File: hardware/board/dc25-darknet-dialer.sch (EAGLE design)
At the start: 80 parts, among them SW1 RESET, X1 USB-MICROB

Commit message: Connected LEDs
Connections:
- net N$57 renamed IR_RCV
- removed net N$46 (its old number): U$2.PC11
- removed net N$47: U$2.PC10
- removed net N$48 (its old number): U$2.PA15
- removed net N$50: U$2.PC9
- removed net N$51: U$2.PC8
- removed net N$52: U$2.PC7
- removed net N$53: U$2.PC6
- removed net N$54: U$2.PC14
- removed net N$58: U$2.PC1
- removed net N$59: U$2.PC2
- removed net N$60: U$2.PC3
- removed net N$61 (its old number): U$2.PB10
- removed net N$62: U$12.LED
- new net OLED_CS: U$12.CS, U$2.PC6
- new net OLED_LED: U$12.LED, U$2.PC7
- net LED1: now also U$2.PC9
- net LED10: now also U$2.PA15
- net LED2: now also U$2.PC8
- net LED3: now also U$2.PB10
- net LED4: now also U$2.PC3
- net LED5: now also U$2.PC2
- net LED6: now also U$2.PC1
- net LED7: now also U$2.PC14
- net LED8: now also U$2.PC11
- net LED9: now also U$2.PC10
- net VCC: no longer U$12.CS

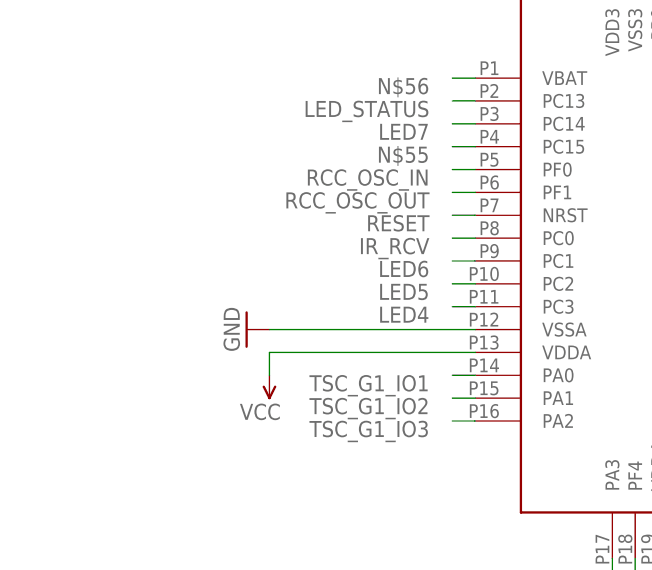
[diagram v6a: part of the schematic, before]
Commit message: Added resonator
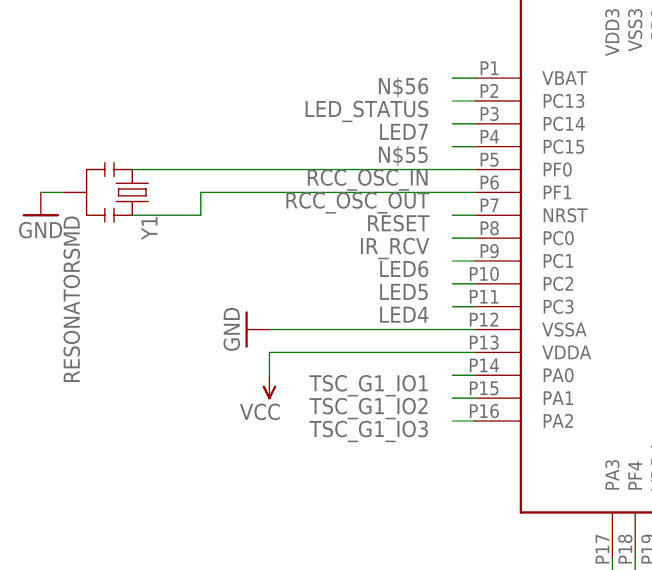
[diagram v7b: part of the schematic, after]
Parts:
- added Y1: RESONATORSMD, SparkFun:RESONATORSMD
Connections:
- net GND: now also Y1.2
- net RCC_OSC_IN: now also Y1.1
- net RCC_OSC_OUT: now also Y1.3
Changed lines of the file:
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@@
 <part name="L1" library="dp_devices" deviceset="FERRITE" device="-0603"/>
 <part name="GND26" library="SYNShop" deviceset="GND" device=""/>
+<part name="Y1" library="SparkFun" deviceset="RESONATOR" device="SMD"/>
+<part name="GND29" library="SYNShop" deviceset="GND" device=""/>
 </parts>
 <sheets>
@@
 <instance part="L1" gate="L" x="15.24" y="363.22" rot="R90"/>
 <instance part="GND26" gate="1" x="33.02" y="355.6"/>
+<instance part="Y1" gate="G$1" x="-43.18" y="104.14" rot="R270"/>
+<instance part="GND29" gate="1" x="-53.34" y="101.6"/>
 </instances>
 <busses>
@@
 <pinref part="SW1" gate="G$1" pin="C"/>
 </segment>
+<segment>
+<pinref part="Y1" gate="G$1" pin="2"/>
+<wire x1="-50.8" y1="104.14" x2="-53.34" y2="104.14" width="0.1524" layer="91"/>
+<pinref part="GND29" gate="1" pin="GND"/>
+</segment>
 </net>
 <net name="N$12" class="0">
@@
 <segment>
 <pinref part="U$2" gate="G$1" pin="PF0"/>
-<wire x1="-5.08" y1="106.68" x2="-7.62" y2="106.68" width="0.1524" layer="91"/>
 <label x="-10.16" y="106.68" size="1.778" layer="95" rot="R180"/>
+<pinref part="Y1" gate="G$1" pin="1"/>
+<wire x1="-5.08" y1="106.68" x2="-43.18" y2="106.68" width="0.1524" layer="91"/>
 </segment>
 </net>
@@
 <segment>
 <pinref part="U$2" gate="G$1" pin="PF1"/>
-<wire x1="-5.08" y1="104.14" x2="-7.62" y2="104.14" width="0.1524" layer="91"/>
 <label x="-10.16" y="104.14" size="1.778" layer="95" rot="R180"/>
-</segment>
-</net>
+<wire x1="-5.08" y1="104.14" x2="-35.56" y2="104.14" width="0.1524" layer="91"/>
+<wire x1="-35.56" y1="104.14" x2="-35.56" y2="101.6" width="0.1524" layer="91"/>
+<pinref part="Y1" gate="G$1" pin="3"/>
+<wire x1="-35.56" y1="101.6" x2="-43.18" y2="101.6" width="0.1524" layer="91"/>
+</segment>
+</net>

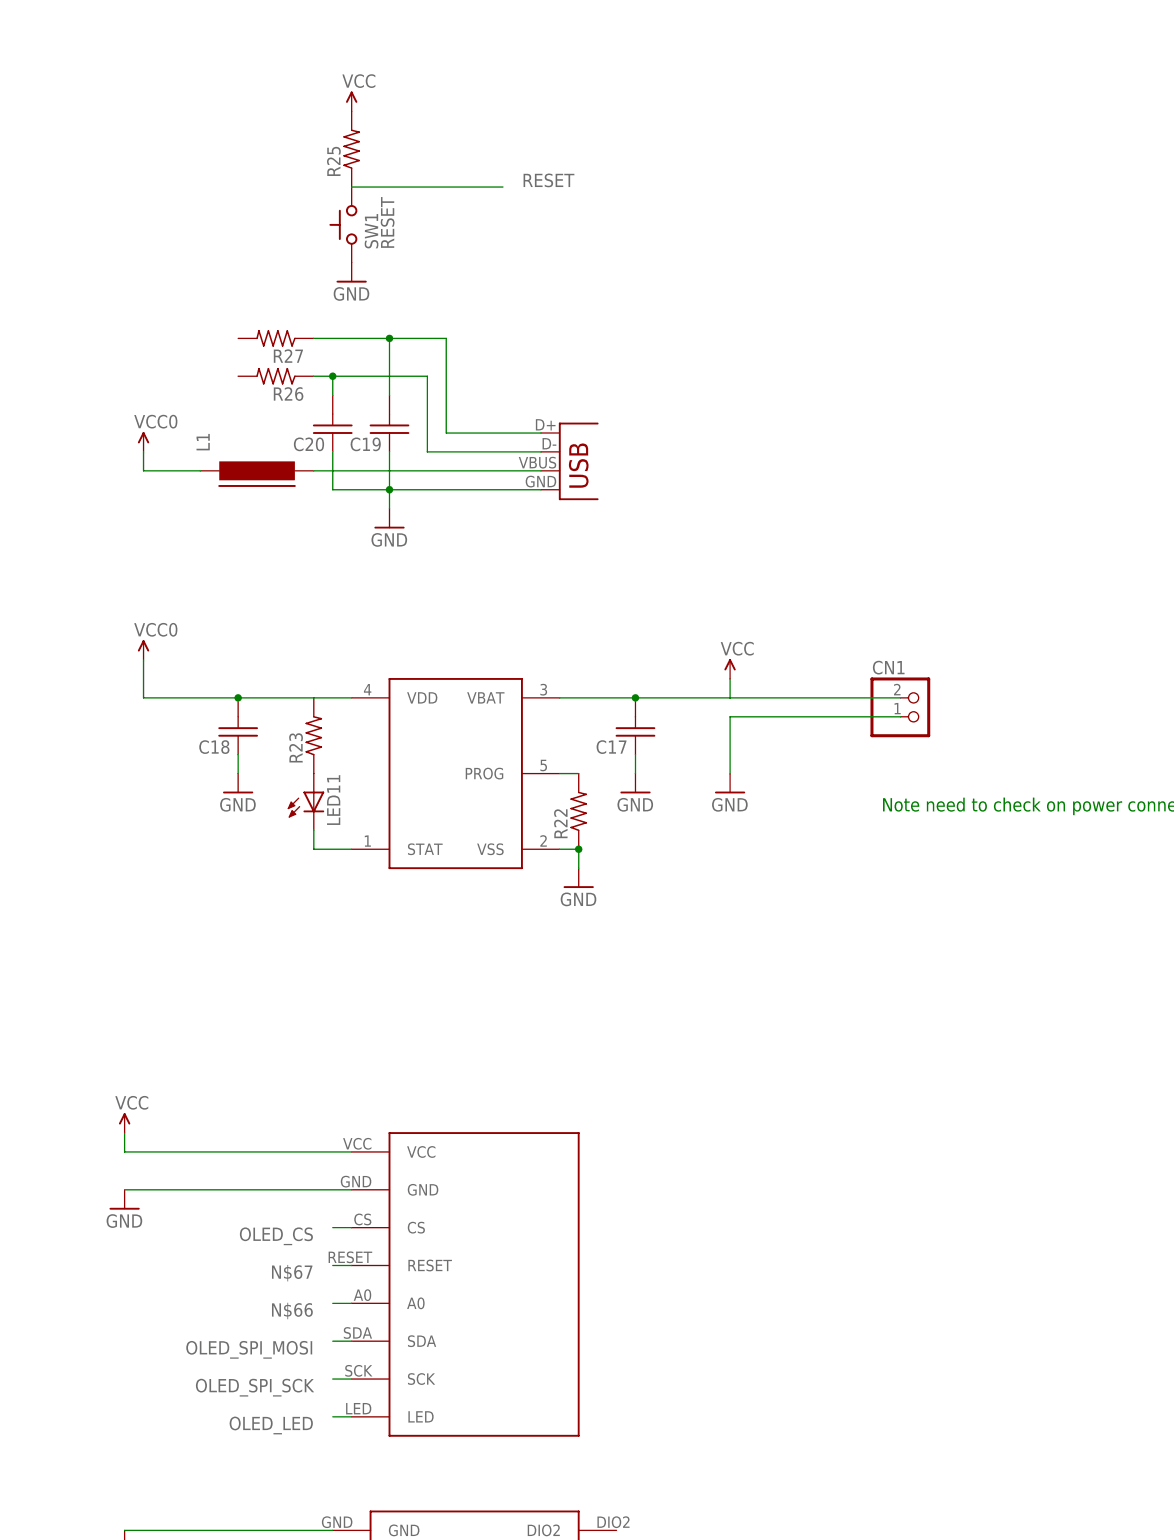
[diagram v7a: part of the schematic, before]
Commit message: Additional details on power, added fuse and prep for 3.3v LDO
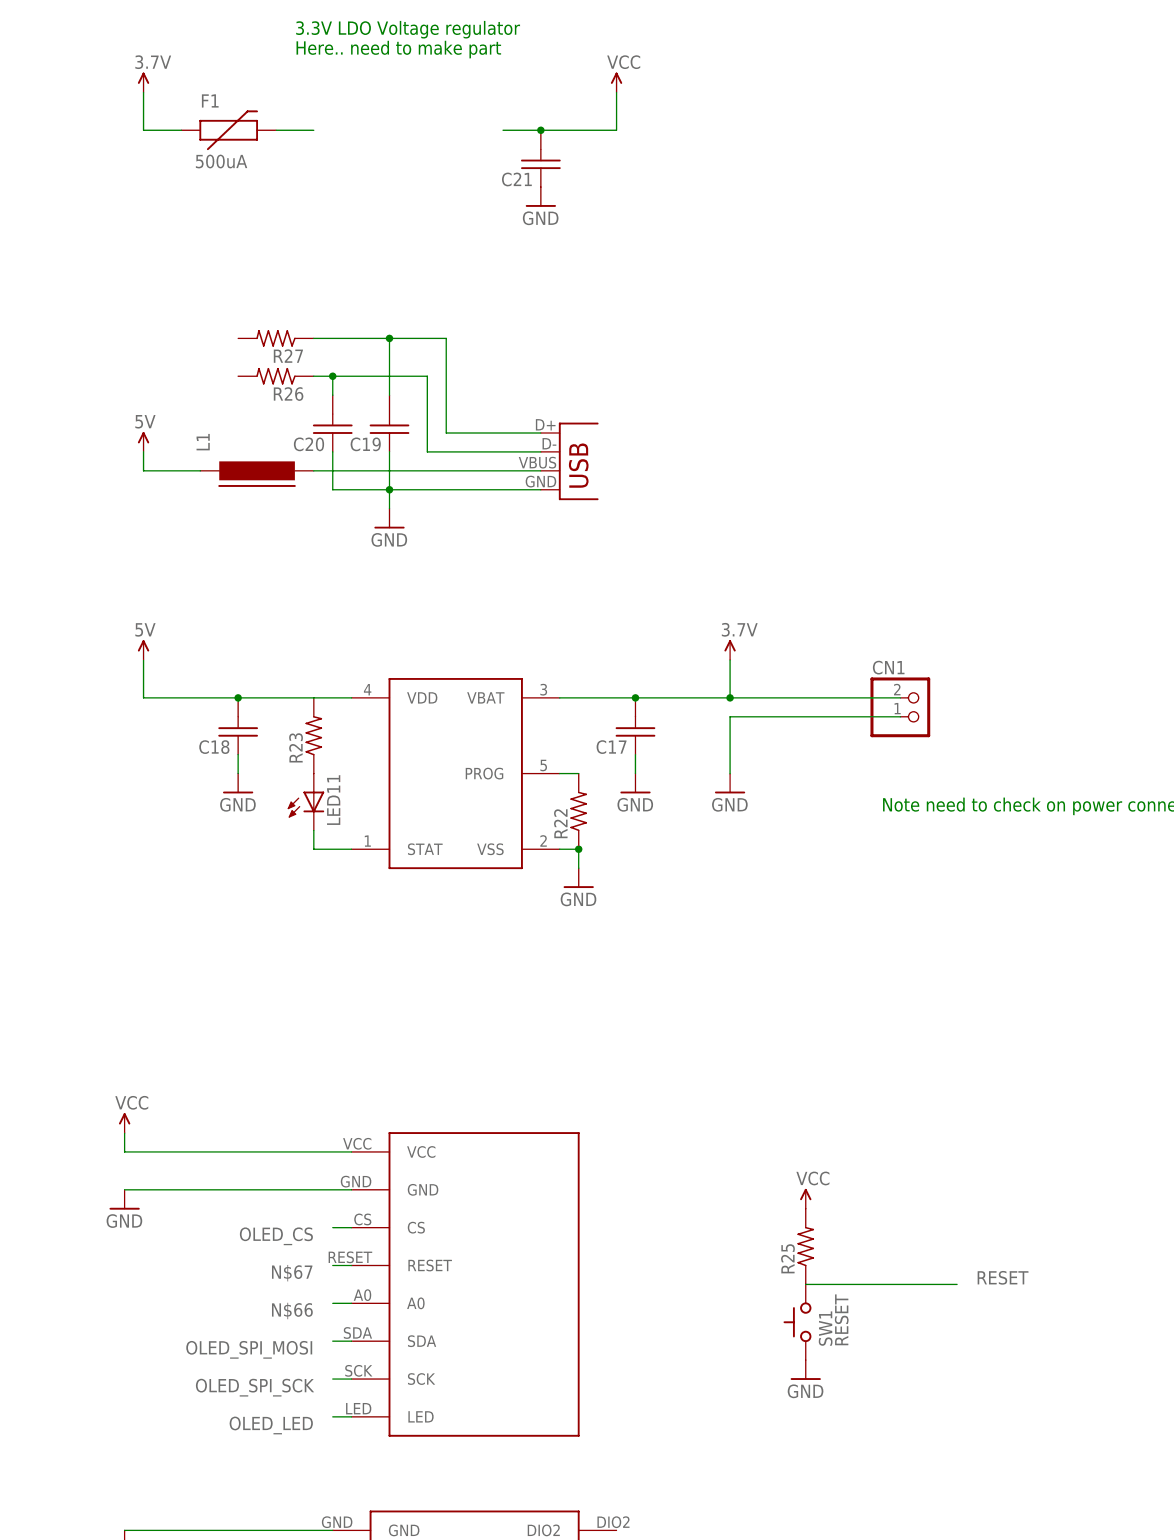
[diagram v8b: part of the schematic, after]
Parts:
- added C21: (no value), SYNShop:C-USC0603
- added F1: 500uA, SparkFun:PTCSMD
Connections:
- new net N$31: F1.2
- new net VCC1: C17.2, CN1.1, F1.1, U$11.VBAT
- net GND: now also C21.1
- net VCC: now also C21.2; no longer C17.2, CN1.1, U$11.VBAT
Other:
- note added: "3.3V LDO Voltage regulator Here.. need to make part"
- moved on the sheet: R25, SW1
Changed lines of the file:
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@@
 <part name="C17" library="SYNShop" deviceset="C-US" device="C0603"/>
 <part name="GND24" library="SYNShop" deviceset="GND" device=""/>
-<part name="U$13" library="SYNShop" deviceset="VCC" device=""/>
-<part name="U$14" library="SYNShop" deviceset="VCC0" device=""/>
+<part name="5V" library="SYNShop" deviceset="VCC0" device="" value="5V"/>
 <part name="C18" library="SYNShop" deviceset="C-US" device="C0603"/>
 <part name="GND25" library="SYNShop" deviceset="GND" device=""/>
 <part name="X1" library="SYNShop" deviceset="USB" device="-MICROB"/>
-<part name="U$16" library="SYNShop" deviceset="VCC0" device=""/>
+<part name="U$16" library="SYNShop" deviceset="VCC0" device="" value="5V"/>
 <part name="U$17" library="SYNShop" deviceset="SOP22" device=""/>
 <part name="LED12" library="SYNShop" deviceset="LED" device="5MM"/>
@@
 <part name="Y1" library="SparkFun" deviceset="RESONATOR" device="SMD"/>
 <part name="GND29" library="SYNShop" deviceset="GND" device=""/>
+<part name="3.7V" library="SYNShop" deviceset="VCC1" device="" value="3.7V"/>
+<part name="F1" library="SparkFun" deviceset="PTC" device="SMD" value="500uA"/>
+<part name="3.7V1" library="SYNShop" deviceset="VCC1" device="" value="3.7V"/>
+<part name="C21" library="SYNShop" deviceset="C-US" device="C0603"/>
+<part name="GND30" library="SYNShop" deviceset="GND" device=""/>
+<part name="U$13" library="SYNShop" deviceset="VCC" device=""/>
 </parts>
 <sheets>
@@
 <plain>
 <text x="99.06" y="317.5" size="1.778" layer="91">Note need to check on power connection / battery</text>
+<text x="20.32" y="419.1" size="1.778" layer="91">3.3V LDO Voltage regulator
+Here.. need to make part</text>
 </plain>
 <instances>
@@
 <instance part="C17" gate="G$1" x="66.04" y="327.66" rot="R180"/>
 <instance part="GND24" gate="1" x="78.74" y="320.04"/>
-<instance part="U$13" gate="G$1" x="78.74" y="335.28"/>
-<instance part="U$14" gate="VCC0" x="0" y="337.82"/>
+<instance part="5V" gate="VCC0" x="0" y="337.82"/>
 <instance part="C18" gate="G$1" x="12.7" y="327.66" rot="R180"/>
 <instance part="GND25" gate="1" x="12.7" y="320.04"/>
@@
 <instance part="U$18" gate="G$1" x="200.66" y="254"/>
 <instance part="CN1" gate="G$1" x="104.14" y="330.2"/>
-<instance part="SW1" gate="G$1" x="27.94" y="396.24"/>
-<instance part="R25" gate="G$1" x="27.94" y="406.4" rot="R90"/>
-<instance part="GND28" gate="1" x="27.94" y="388.62"/>
-<instance part="U$20" gate="G$1" x="27.94" y="411.48"/>
+<instance part="SW1" gate="G$1" x="88.9" y="248.92"/>
+<instance part="R25" gate="G$1" x="88.9" y="259.08" rot="R90"/>
+<instance part="GND28" gate="1" x="88.9" y="241.3"/>
+<instance part="U$20" gate="G$1" x="88.9" y="264.16"/>
 <instance part="R26" gate="G$1" x="17.78" y="375.92" rot="R180"/>
 <instance part="R27" gate="G$1" x="17.78" y="381" rot="R180"/>
@@
 <instance part="Y1" gate="G$1" x="-43.18" y="104.14" rot="R270"/>
 <instance part="GND29" gate="1" x="-53.34" y="101.6"/>
+<instance part="3.7V" gate="G$1" x="78.74" y="337.82"/>
+<instance part="F1" gate="G$1" x="10.16" y="408.94"/>
+<instance part="3.7V1" gate="G$1" x="0" y="414.02"/>
+<instance part="C21" gate="G$1" x="53.34" y="403.86" rot="R180"/>
+<instance part="GND30" gate="1" x="53.34" y="398.78"/>
+<instance part="U$13" gate="G$1" x="63.5" y="414.02"/>
 </instances>
 <busses>
@@
 <pinref part="GND29" gate="1" pin="GND"/>
 </segment>
+<segment>
+<pinref part="C21" gate="G$1" pin="1"/>
+<pinref part="GND30" gate="1" pin="GND"/>
+</segment>
 </net>
 <net name="N$12" class="0">
@@
 <pinref part="R25" gate="G$1" pin="1"/>
 <pinref part="SW1" gate="G$1" pin="A"/>
-<wire x1="27.94" y1="401.32" x2="48.26" y2="401.32" width="0.1524" layer="91"/>
-<label x="50.8" y="401.32" size="1.778" layer="95"/>
+<wire x1="88.9" y1="254" x2="109.22" y2="254" width="0.1524" layer="91"/>
+<label x="111.76" y="254" size="1.778" layer="95"/>
 </segment>
 </net>
@@
 </segment>
 <segment>
-<pinref part="U$11" gate="G$1" pin="VBAT"/>
-<wire x1="55.88" y1="332.74" x2="66.04" y2="332.74" width="0.1524" layer="91"/>
-<pinref part="C17" gate="G$1" pin="2"/>
-<wire x1="66.04" y1="332.74" x2="78.74" y2="332.74" width="0.1524" layer="91"/>
-<junction x="66.04" y="332.74"/>
-<pinref part="U$13" gate="G$1" pin="VCC"/>
-<wire x1="78.74" y1="332.74" x2="78.74" y2="335.28" width="0.1524" layer="91"/>
-<pinref part="CN1" gate="G$1" pin="1"/>
-<wire x1="78.74" y1="332.74" x2="101.6" y2="332.74" width="0.1524" layer="91"/>
-</segment>
-<segment>
 <pinref part="U$17" gate="G$1" pin="VS"/>
 <pinref part="U$18" gate="G$1" pin="VCC"/>
@@
 <pinref part="R25" gate="G$1" pin="2"/>
 <pinref part="U$20" gate="G$1" pin="VCC"/>
+</segment>
+<segment>
+<pinref part="C21" gate="G$1" pin="2"/>
+<wire x1="53.34" y1="408.94" x2="63.5" y2="408.94" width="0.1524" layer="91"/>
+<wire x1="63.5" y1="408.94" x2="63.5" y2="414.02" width="0.1524" layer="91"/>
+<pinref part="U$13" gate="G$1" pin="VCC"/>
+<wire x1="53.34" y1="408.94" x2="48.26" y2="408.94" width="0.1524" layer="91"/>
+<junction x="53.34" y="408.94"/>
 </segment>
 </net>
@@
 <junction x="12.7" y="332.74"/>
 <wire x1="12.7" y1="332.74" x2="0" y2="332.74" width="0.1524" layer="91"/>
-<pinref part="U$14" gate="VCC0" pin="VCC0"/>
+<pinref part="5V" gate="VCC0" pin="VCC0"/>
 <wire x1="0" y1="332.74" x2="0" y2="337.82" width="0.1524" layer="91"/>
 </segment>
@@
 </segment>
 </net>
+<net name="VCC1" class="0">
+<segment>
+<pinref part="U$11" gate="G$1" pin="VBAT"/>
+<wire x1="55.88" y1="332.74" x2="66.04" y2="332.74" width="0.1524" layer="91"/>
+<pinref part="C17" gate="G$1" pin="2"/>
+<wire x1="66.04" y1="332.74" x2="78.74" y2="332.74" width="0.1524" layer="91"/>
+<junction x="66.04" y="332.74"/>
+<wire x1="78.74" y1="332.74" x2="78.74" y2="337.82" width="0.1524" layer="91"/>
+<pinref part="CN1" gate="G$1" pin="1"/>
+<wire x1="78.74" y1="332.74" x2="101.6" y2="332.74" width="0.1524" layer="91"/>
+<pinref part="3.7V" gate="G$1" pin="VCC1"/>
+<junction x="78.74" y="332.74"/>
+</segment>
+<segment>
+<pinref part="F1" gate="G$1" pin="1"/>
+<wire x1="5.08" y1="408.94" x2="0" y2="408.94" width="0.1524" layer="91"/>
+<pinref part="3.7V1" gate="G$1" pin="VCC1"/>
+<wire x1="0" y1="408.94" x2="0" y2="414.02" width="0.1524" layer="91"/>
+</segment>
+</net>
+<net name="N$31" class="0">
+<segment>
+<pinref part="F1" gate="G$1" pin="2"/>
+<wire x1="17.78" y1="408.94" x2="22.86" y2="408.94" width="0.1524" layer="91"/>
+</segment>
+</net>
 </nets>
 </sheet>
@@
 </schematic>
 </drawing>
+<compatibility>
+<note version="6.3" minversion="6.2.2" severity="warning">
+Since Version 6.2.2 text objects can contain more than one line,
+which will not be processed correctly with this version.
+</note>
+</compatibility>
 </eagle>
